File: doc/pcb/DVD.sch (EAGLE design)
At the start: 30 parts, among them IC1 7805, IC2 74HC14N

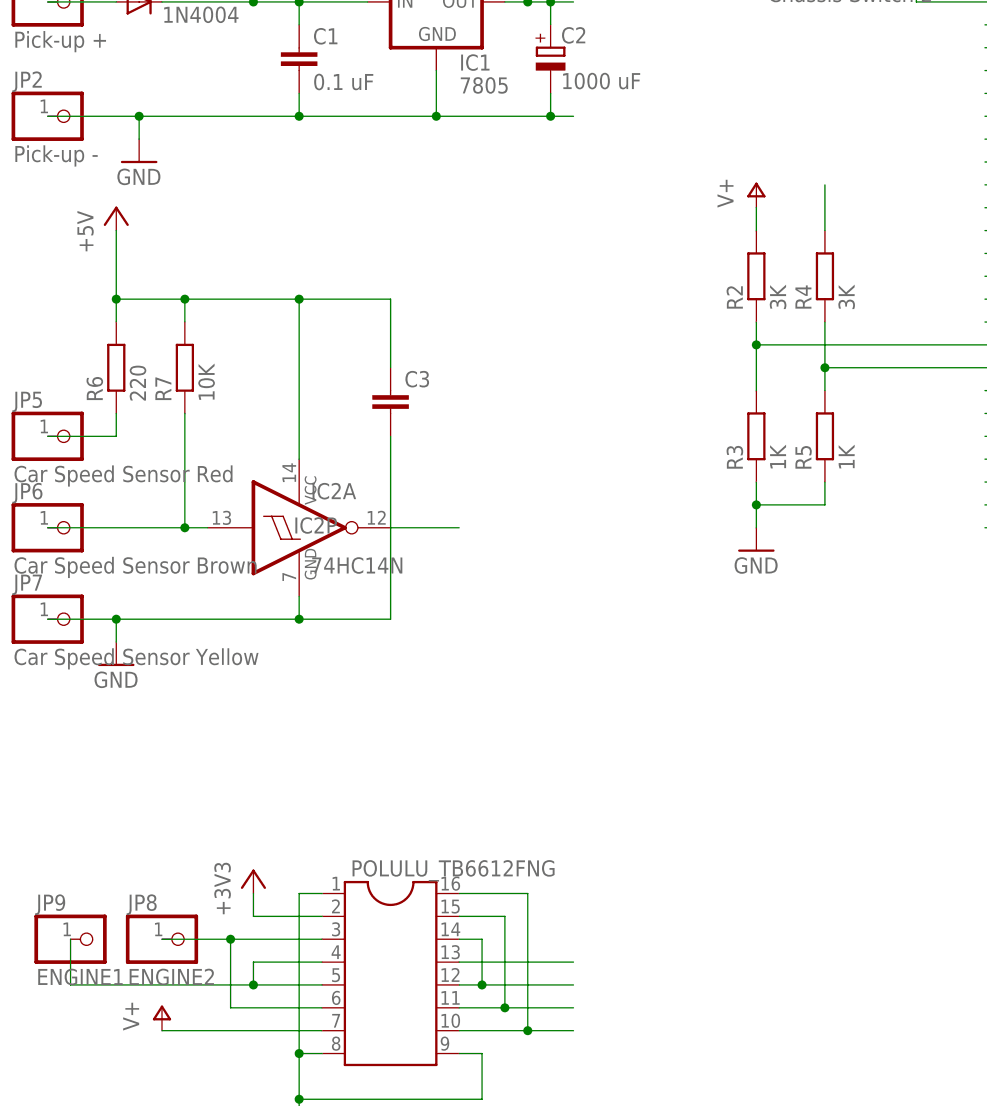
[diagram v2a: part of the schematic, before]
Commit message: PCB Update
Added connection from Pololu to voltage measuring resistors
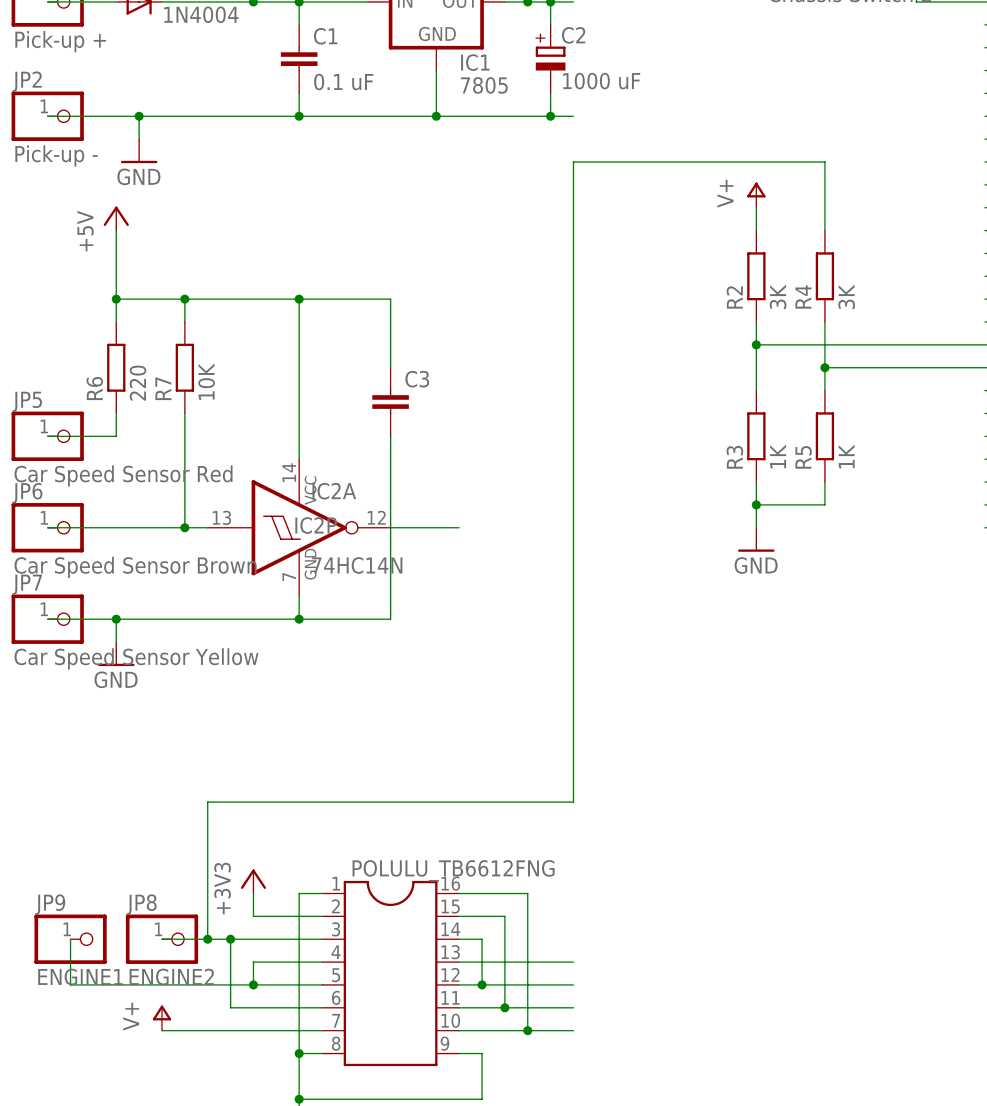
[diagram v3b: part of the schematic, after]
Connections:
- removed net N$29: R4.2
- net JP8: now also R4.2
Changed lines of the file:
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@@
-</segment>
-</net>
-<net name="N$29" class="0">
-<segment>
-<pinref part="R4" gate="G$1" pin="2"/>
-<wire x1="68.58" y1="114.3" x2="68.58" y2="119.38" width="0.1524" layer="91"/>
 </segment>
 </net>
@@
 <wire x1="12.7" y1="35.56" x2="2.54" y2="35.56" width="0.1524" layer="91"/>
 <junction x="2.54" y="35.56"/>
-<wire x1="2.54" y1="35.56" x2="-5.08" y2="35.56" width="0.1524" layer="91"/>
+<wire x1="2.54" y1="35.56" x2="0" y2="35.56" width="0.1524" layer="91"/>
+<pinref part="R4" gate="G$1" pin="2"/>
+<wire x1="0" y1="35.56" x2="-5.08" y2="35.56" width="0.1524" layer="91"/>
+<wire x1="68.58" y1="114.3" x2="68.58" y2="121.92" width="0.1524" layer="91"/>
+<wire x1="68.58" y1="121.92" x2="40.64" y2="121.92" width="0.1524" layer="91"/>
+<wire x1="40.64" y1="121.92" x2="40.64" y2="50.8" width="0.1524" layer="91"/>
+<wire x1="40.64" y1="50.8" x2="0" y2="50.8" width="0.1524" layer="91"/>
+<wire x1="0" y1="50.8" x2="0" y2="35.56" width="0.1524" layer="91"/>
+<junction x="0" y="35.56"/>
 </segment>
 </net>

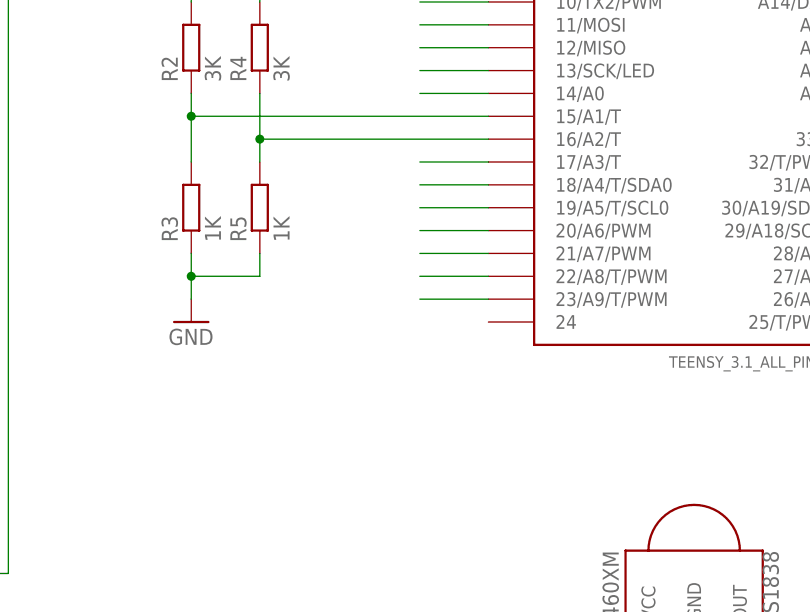
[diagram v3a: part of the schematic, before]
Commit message: Added engine temperature measurement pin
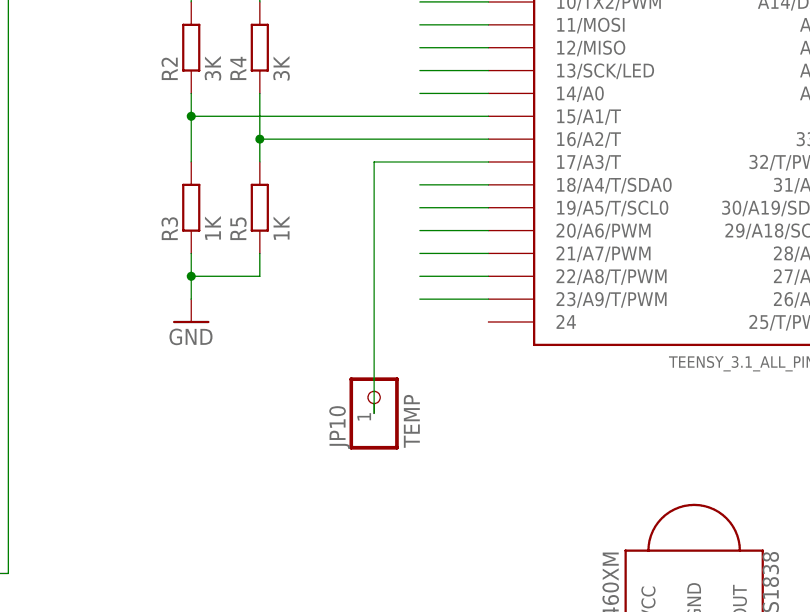
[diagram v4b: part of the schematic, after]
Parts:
- added JP10: TEMP, pinhead:PINHD-1X1
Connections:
- removed net N$24: U$1.17/A3/T
- new net JP0: JP10.1, U$1.17/A3/T
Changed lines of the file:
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@@
 <part name="C3" library="resistor" deviceset="C-EU" device="025-025X050"/>
 <part name="C4" library="resistor" deviceset="C-EU" device="025-025X050"/>
+<part name="JP10" library="pinhead" deviceset="PINHD-1X1" device="" value="TEMP"/>
 </parts>
 <sheets>
@@
 <instance part="C3" gate="G$1" x="20.32" y="96.52"/>
 <instance part="C4" gate="G$1" x="190.5" y="93.98" rot="R90"/>
+<instance part="JP10" gate="G$1" x="81.28" y="71.12" rot="R90"/>
 </instances>
 <busses>
@@
 </segment>
 </net>
-<net name="N$24" class="0">
+<net name="JP0" class="0">
 <segment>
 <pinref part="U$1" gate="G$1" pin="17/A3/T"/>
-<wire x1="93.98" y1="96.52" x2="86.36" y2="96.52" width="0.1524" layer="91"/>
-</segment>
-</net>
+<wire x1="93.98" y1="96.52" x2="81.28" y2="96.52" width="0.1524" layer="91"/>
+<pinref part="JP10" gate="G$1" pin="1"/>
+<wire x1="81.28" y1="68.58" x2="81.28" y2="96.52" width="0.1524" layer="91"/>
+</segment>
+</net>

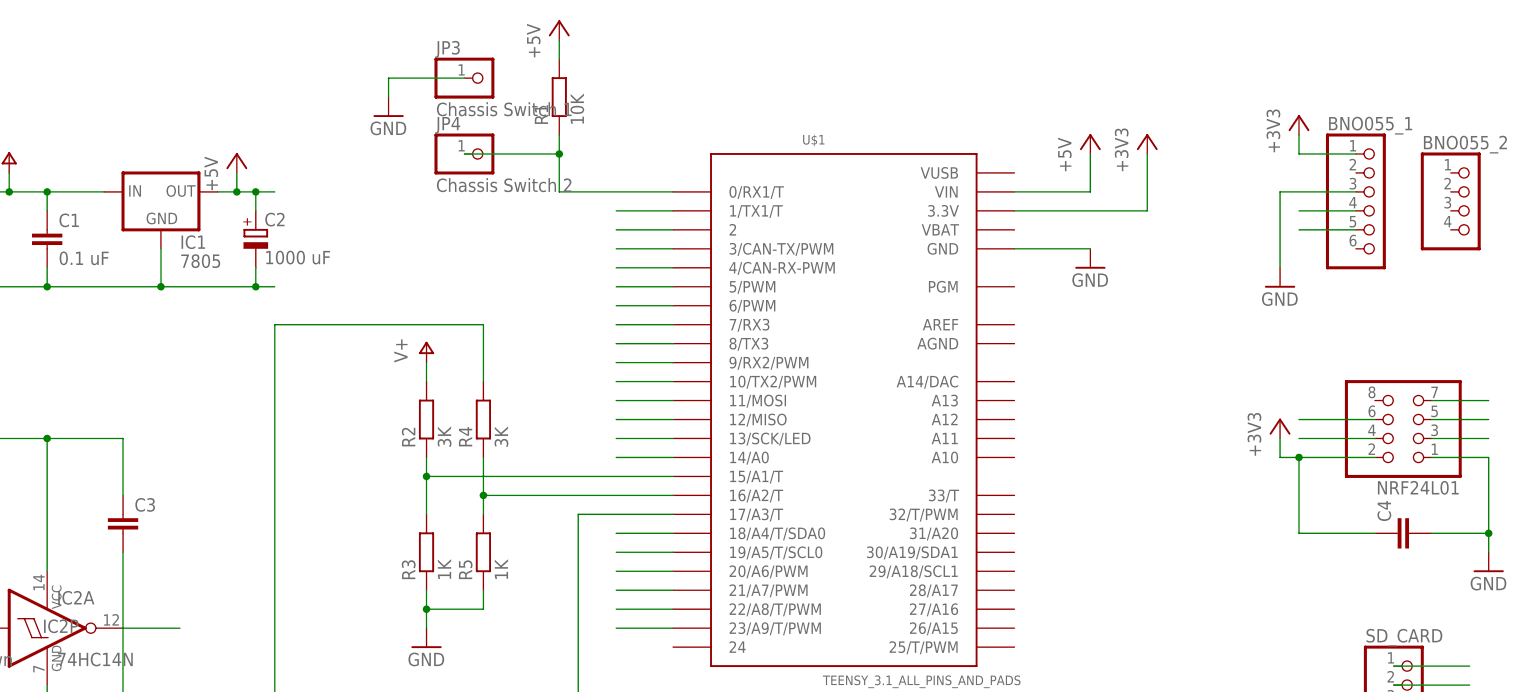
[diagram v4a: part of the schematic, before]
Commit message: Cleaned up parts of TODO list
- declared STBY as ouput
- added Diodes in Teensy input
- ...
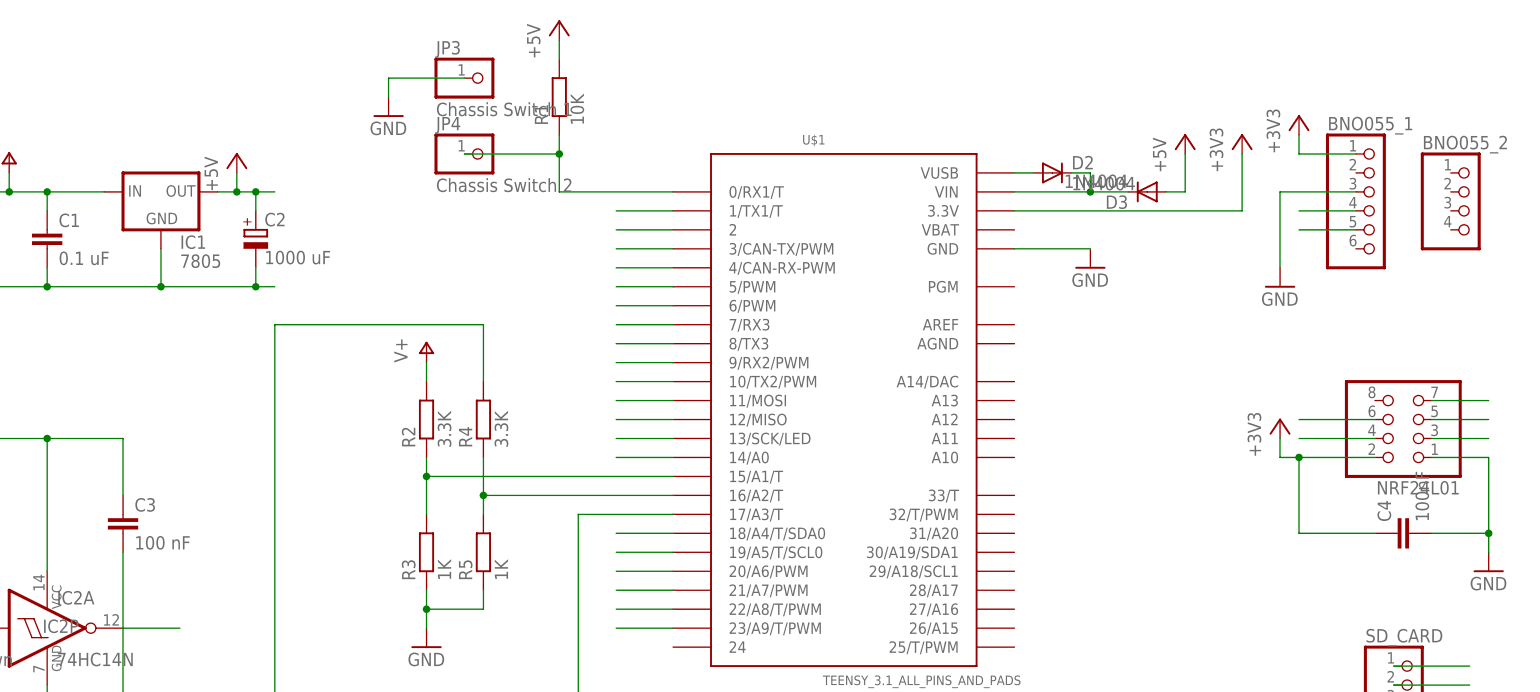
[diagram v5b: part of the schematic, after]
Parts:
- added D2, D3: 1N4004, adafruit:1N4004
- C3: value (none) -> 100 nF
- C4: value (none) -> 100nF
- R2, R4: value 3K -> 3.3K
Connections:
- new net N$1: D2.C, D3.C, U$1.VIN
- new net N$4: D2.A, U$1.VUSB
- net +5V: now also D3.A; no longer U$1.VIN
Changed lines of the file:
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@@
 <part name="+3V1" library="supply1" deviceset="+3V3" device=""/>
 <part name="R1" library="resistor" deviceset="R-EU_" device="0204/7" value="10K"/>
-<part name="R2" library="resistor" deviceset="R-EU_" device="0204/7" value="3K"/>
+<part name="R2" library="resistor" deviceset="R-EU_" device="0204/7" value="3.3K"/>
 <part name="R3" library="resistor" deviceset="R-EU_" device="0204/7" value="1K"/>
-<part name="R4" library="resistor" deviceset="R-EU_" device="0204/7" value="3K"/>
+<part name="R4" library="resistor" deviceset="R-EU_" device="0204/7" value="3.3K"/>
 <part name="R5" library="resistor" deviceset="R-EU_" device="0204/7" value="1K"/>
 <part name="R6" library="resistor" deviceset="R-EU_" device="0204/7" value="220"/>
@@
 <part name="P+11" library="supply1" deviceset="V+" device=""/>
 <part name="C2" library="resistor" deviceset="CPOL-EU" device="P128-50" value="1000 uF"/>
-<part name="C3" library="resistor" deviceset="C-EU" device="025-025X050"/>
-<part name="C4" library="resistor" deviceset="C-EU" device="025-025X050"/>
+<part name="C3" library="resistor" deviceset="C-EU" device="025-025X050" value="100 nF"/>
+<part name="C4" library="resistor" deviceset="C-EU" device="025-025X050" value="100nF"/>
 <part name="JP10" library="pinhead" deviceset="PINHD-1X1" device="" value="TEMP"/>
+<part name="D2" library="adafruit" deviceset="1N4004" device=""/>
+<part name="D3" library="adafruit" deviceset="1N4004" device=""/>
 </parts>
 <sheets>
@@
 <instance part="D1" gate="1" x="-7.62" y="139.7"/>
 <instance part="P+2" gate="1" x="35.56" y="144.78"/>
-<instance part="P+3" gate="1" x="149.86" y="147.32"/>
+<instance part="P+3" gate="1" x="162.56" y="147.32"/>
 <instance part="GND2" gate="1" x="149.86" y="129.54"/>
 <instance part="JP3" gate="G$1" x="68.58" y="154.94"/>
@@
 <instance part="GND6" gate="1" x="-10.16" y="66.04"/>
 <instance part="GND7" gate="1" x="200.66" y="58.42"/>
-<instance part="+3V1" gate="G$1" x="157.48" y="147.32"/>
+<instance part="+3V1" gate="G$1" x="170.18" y="147.32"/>
 <instance part="R1" gate="G$1" x="78.74" y="152.4" rot="R90"/>
 <instance part="R2" gate="G$1" x="60.96" y="109.22" rot="R90"/>
@@
 <instance part="C4" gate="G$1" x="190.5" y="93.98" rot="R90"/>
 <instance part="JP10" gate="G$1" x="81.28" y="71.12" rot="R90"/>
+<instance part="D2" gate="1" x="144.78" y="142.24"/>
+<instance part="D3" gate="1" x="157.48" y="139.7" rot="R180"/>
 </instances>
 <busses>
@@
 </segment>
 <segment>
-<pinref part="U$1" gate="G$1" pin="VIN"/>
-<pinref part="P+3" gate="1" pin="+5V"/>
-<wire x1="139.7" y1="139.7" x2="149.86" y2="139.7" width="0.1524" layer="91"/>
-<wire x1="149.86" y1="139.7" x2="149.86" y2="144.78" width="0.1524" layer="91"/>
-</segment>
-<segment>
 <pinref part="VS1838" gate="G$1" pin="VCC"/>
 <pinref part="P+4" gate="1" pin="+5V"/>
@@
 <pinref part="P+8" gate="1" pin="+5V"/>
 </segment>
+<segment>
+<pinref part="P+3" gate="1" pin="+5V"/>
+<wire x1="162.56" y1="144.78" x2="162.56" y2="139.7" width="0.1524" layer="91"/>
+<pinref part="D3" gate="1" pin="A"/>
+<wire x1="162.56" y1="139.7" x2="160.02" y2="139.7" width="0.1524" layer="91"/>
+</segment>
 </net>
 <net name="D4_IR" class="0">
@@
 <segment>
 <pinref part="U$1" gate="G$1" pin="3.3V"/>
-<wire x1="139.7" y1="137.16" x2="157.48" y2="137.16" width="0.1524" layer="91"/>
+<wire x1="139.7" y1="137.16" x2="170.18" y2="137.16" width="0.1524" layer="91"/>
 <pinref part="+3V1" gate="G$1" pin="+3V3"/>
-<wire x1="157.48" y1="137.16" x2="157.48" y2="144.78" width="0.1524" layer="91"/>
+<wire x1="170.18" y1="137.16" x2="170.18" y2="144.78" width="0.1524" layer="91"/>
 </segment>
 <segment>
@@
 </segment>
 </net>
+<net name="N$1" class="0">
+<segment>
+<pinref part="D3" gate="1" pin="C"/>
+<pinref part="U$1" gate="G$1" pin="VIN"/>
+<wire x1="154.94" y1="139.7" x2="149.86" y2="139.7" width="0.1524" layer="91"/>
+<pinref part="D2" gate="1" pin="C"/>
+<wire x1="149.86" y1="139.7" x2="139.7" y2="139.7" width="0.1524" layer="91"/>
+<wire x1="147.32" y1="142.24" x2="149.86" y2="142.24" width="0.1524" layer="91"/>
+<wire x1="149.86" y1="142.24" x2="149.86" y2="139.7" width="0.1524" layer="91"/>
+<junction x="149.86" y="139.7"/>
+</segment>
+</net>
+<net name="N$4" class="0">
+<segment>
+<pinref part="U$1" gate="G$1" pin="VUSB"/>
+<pinref part="D2" gate="1" pin="A"/>
+<wire x1="139.7" y1="142.24" x2="142.24" y2="142.24" width="0.1524" layer="91"/>
+</segment>
+</net>
